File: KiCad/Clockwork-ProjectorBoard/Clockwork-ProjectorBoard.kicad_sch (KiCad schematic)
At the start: 32 parts, among them J1 to TCA955 PCB, J2 to DIN connecting 3+1 Socket 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, J3 to Lamp Relay Board, J4 to DIN Socket traces, J5 Relais Board, J6 uC Cable, J7 DIN-6 female, Q1 AO3400A, U1 AP63205WU, U3 TS5A3160DBVR-TP, U4 TS5A3160DBVR-TP, U5 TSV911ILT

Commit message: Renaming once more
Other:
- title: SynCrystal Projector Board T610/T525 -> Clockwork Projector Board T610/T525
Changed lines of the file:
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@@
 	(paper "A4")
 	(title_block
-		(title "SynCrystal Projector Board T610/T525")
-		(date "2025-02-11")
+		(title "Clockwork Projector Board T610/T525")
+		(date "2025-04-02")
 		(rev "Rev.A")
 		(company "filmkorn.org")

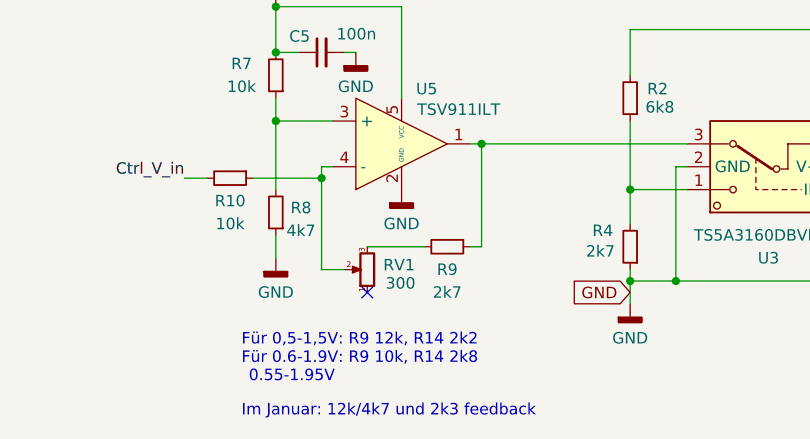
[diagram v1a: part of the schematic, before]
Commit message: New Gerbers, added the xtal to the BOM, new MH for OLED
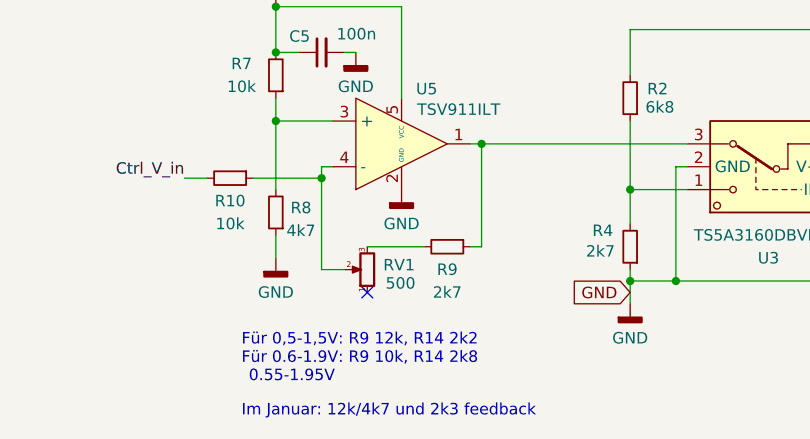
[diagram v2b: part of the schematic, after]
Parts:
- J2: LCSC C5188443 -> C6332196
- J6: footprint Connector_PinHeader_2.54mm:PinHeader_1x10_P2.54mm_Horizontal -> easyEDA:HDR-TH_10P-P2.54-H-M-W10.4_flipped; LCSC (none) -> C3012231
- R1: LCSC (none) -> C22962
- R2: LCSC (none) -> C23212
- R3: LCSC (none) -> C23189
- RV1: value 300 -> 500; LCSC C22461623 -> C720649; LCSC Part (none) -> C22461623
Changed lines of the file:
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@@
 			)
 		)
-		(property "LCSC" "C5188443"
+		(property "LCSC" "C6332196"
 			(at 57.15 33.02 0)
 			(effects
@@
 			)
 		)
-		(property "Datasheet" "~"
+		(property "Datasheet" "https://www.lcsc.com/datasheet/lcsc_datasheet_2411221126_UNI-ROYAL-Uniroyal-Elec-0603WAF2200T5E_C22962.pdf"
 			(at 223.52 119.38 0)
 			(effects
@@
 		)
 		(property "Description" ""
+			(at 223.52 119.38 0)
+			(effects
+				(font
+					(size 1.27 1.27)
+				)
+				(hide yes)
+			)
+		)
+		(property "LCSC" "C22962"
 			(at 223.52 119.38 0)
 			(effects
@@
 			)
 		)
-		(property "Value" "300"
+		(property "Value" "500"
 			(at 79.502 141.224 0)
 			(effects
@@
 			)
 		)
-		(property "Datasheet" "~"
+		(property "Datasheet" "https://www.lcsc.com/datasheet/lcsc_datasheet_2409302333_BOURNS-TC33X-2-501E_C720649.pdf"
 			(at 77.47 139.7 0)
 			(effects
@@
 			)
 		)
-		(property "LCSC" "C22461623"
+		(property "LCSC" "C720649"
+			(at 77.47 139.7 0)
+			(effects
+				(font
+					(size 1.27 1.27)
+				)
+				(hide yes)
+			)
+		)
+		(property "LCSC Part" "C22461623"
 			(at 77.47 139.7 0)
 			(effects
@@
 			)
 		)
-		(property "Footprint" "Connector_PinHeader_2.54mm:PinHeader_1x10_P2.54mm_Horizontal"
+		(property "Footprint" "easyEDA:HDR-TH_10P-P2.54-H-M-W10.4_flipped"
 			(at 254 138.43 0)
 			(effects
@@
 		)
 		(property "Description" "Generic connector, single row, 01x10, script generated"
+			(at 254 138.43 0)
+			(effects
+				(font
+					(size 1.27 1.27)
+				)
+				(hide yes)
+			)
+		)
+		(property "LCSC" "C3012231"
 			(at 254 138.43 0)
 			(effects
@@
 			)
 		)
+		(property "LCSC" "C23212"
+			(at 106.68 120.65 0)
+			(effects
+				(font
+					(size 1.27 1.27)
+				)
+				(hide yes)
+			)
+		)
 		(pin "1"
 		)
@@
 			(at 138.43 125.73 0)
 			(effects
+				(font
+					(size 1.27 1.27)
+				)
+				(hide yes)
+			)
+		)
+		(property "LCSC" "C23189"
+			(at 138.43 125.73 0)
+			(effects

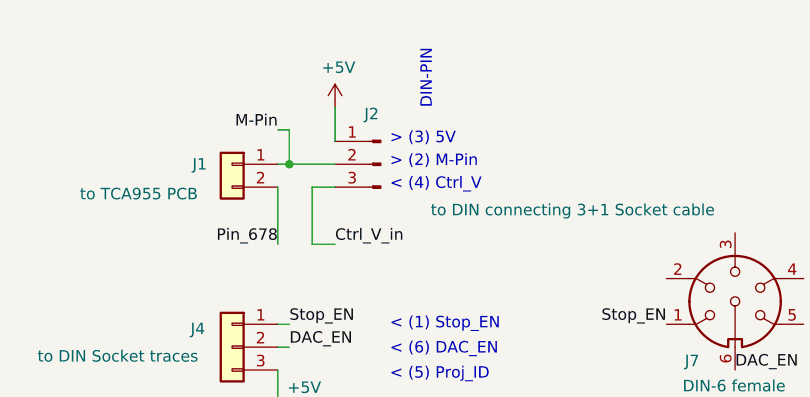
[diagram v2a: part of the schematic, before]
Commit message: Starting Rev.B, fixing DIN-Connector-Wire Pin 2/3 to keep DIN/JST pin alignment
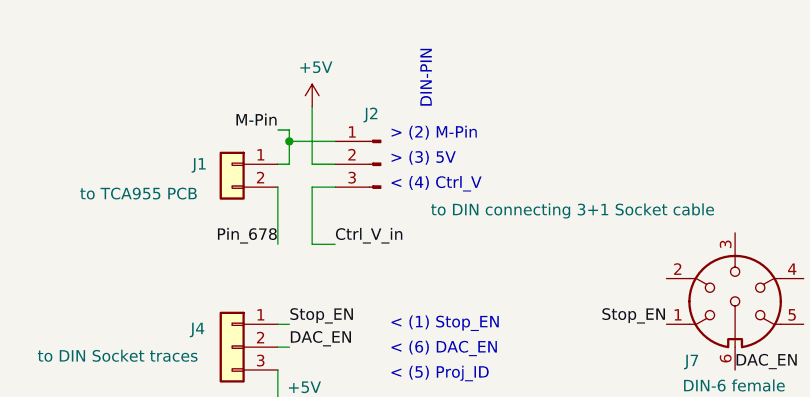
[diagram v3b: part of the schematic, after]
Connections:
- net +5V: now also J2.2 (Pin_2); no longer J2.1 (Pin_1)
- net M-Pin: now also J2.1 (Pin_1); no longer J2.2 (Pin_2)
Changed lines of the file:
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@@
 	)
 	(junction
-		(at 46.99 33.02)
-		(diameter 0)
-		(color 0 0 0 0)
-	)
-	(junction
 		(at 166.37 30.48)
 		(diameter 0)
@@
 	)
 	(junction
+		(at 46.99 30.48)
+		(diameter 0)
+		(color 0 0 0 0)
+	)
+	(junction
 		(at 167.64 130.81)
 		(diameter 0)
@@
 	(wire
 		(pts
-			(xy 90.17 125.73) (xy 88.9 125.73)
+			(xy 49.53 26.67) (xy 49.53 33.02)
 		)
 		(stroke
@@
 	(wire
 		(pts
-			(xy 246.38 114.3) (xy 246.38 121.92)
+			(xy 90.17 125.73) (xy 88.9 125.73)
 		)
 		(stroke
@@
 	(wire
 		(pts
-			(xy 254 102.87) (xy 254 133.35)
+			(xy 246.38 114.3) (xy 246.38 121.92)
 		)
 		(stroke
@@
 	(wire
 		(pts
-			(xy 172.72 30.48) (xy 173.99 30.48)
+			(xy 254 102.87) (xy 254 133.35)
 		)
 		(stroke
@@
 	(wire
 		(pts
-			(xy 46.99 33.02) (xy 52.07 33.02)
+			(xy 172.72 30.48) (xy 173.99 30.48)
 		)
 		(stroke
@@
 	(wire
 		(pts
+			(xy 46.99 30.48) (xy 46.99 33.02)
+		)
+		(stroke
+			(width 0)
+			(type default)
+		)
+	)
+	(wire
+		(pts
 			(xy 72.39 129.54) (xy 72.39 128.27)
 		)
@@
 	(wire
 		(pts
+			(xy 46.99 30.48) (xy 52.07 30.48)
+		)
+		(stroke
+			(width 0)
+			(type default)
+		)
+	)
+	(wire
+		(pts
 			(xy 72.39 128.27) (xy 73.66 128.27)
 		)
@@
 	(wire
 		(pts
+			(xy 49.53 33.02) (xy 52.07 33.02)
+		)
+		(stroke
+			(width 0)
+			(type default)
+		)
+	)
+	(wire
+		(pts
 			(xy 67.31 110.49) (xy 67.31 115.57)
 		)
@@
 	(wire
 		(pts
-			(xy 52.07 30.48) (xy 52.07 26.67)
-		)
-		(stroke
-			(width 0)
-			(type default)
-		)
-	)
-	(wire
-		(pts
 			(xy 143.51 43.18) (xy 152.4 43.18)
 		)
@@
 	(wire
 		(pts
-			(xy 46.99 29.21) (xy 46.99 33.02)
+			(xy 46.99 29.21) (xy 46.99 30.48)
 		)
 		(stroke
@@
 	(text "> (3) 5V"
 		(exclude_from_sim no)
-		(at 58.166 30.226 0)
+		(at 58.166 32.512 0)
 		(effects
 			(font
@@
 	(text "> (2) M-Pin"
 		(exclude_from_sim no)
-		(at 58.166 32.766 0)
+		(at 58.166 29.718 0)
 		(effects
 			(font
@@
 	(symbol
 		(lib_id "power:+5V")
-		(at 52.07 26.67 0)
+		(at 49.53 26.67 0)
 		(unit 1)
 		(exclude_from_sim no)
@@
 		(dnp no)
 		(property "Reference" "#PWR01"
-			(at 52.07 30.48 0)
+			(at 49.53 30.48 0)
 			(effects
 				(font
@@
 		)
 		(property "Value" "+5V"
-			(at 52.451 22.2758 0)
+			(at 49.911 22.2758 0)
 			(effects
 				(font
@@
 		)
 		(property "Footprint" ""
-			(at 52.07 26.67 0)
+			(at 49.53 26.67 0)
 			(effects
 				(font
@@
 		)
 		(property "Datasheet" ""
-			(at 52.07 26.67 0)
+			(at 49.53 26.67 0)
 			(effects
 				(font
@@
 		)
 		(property "Description" "Power symbol creates a global label with name \"+5V\""
-			(at 52.07 26.67 0)
+			(at 49.53 26.67 0)
 			(effects
 				(font

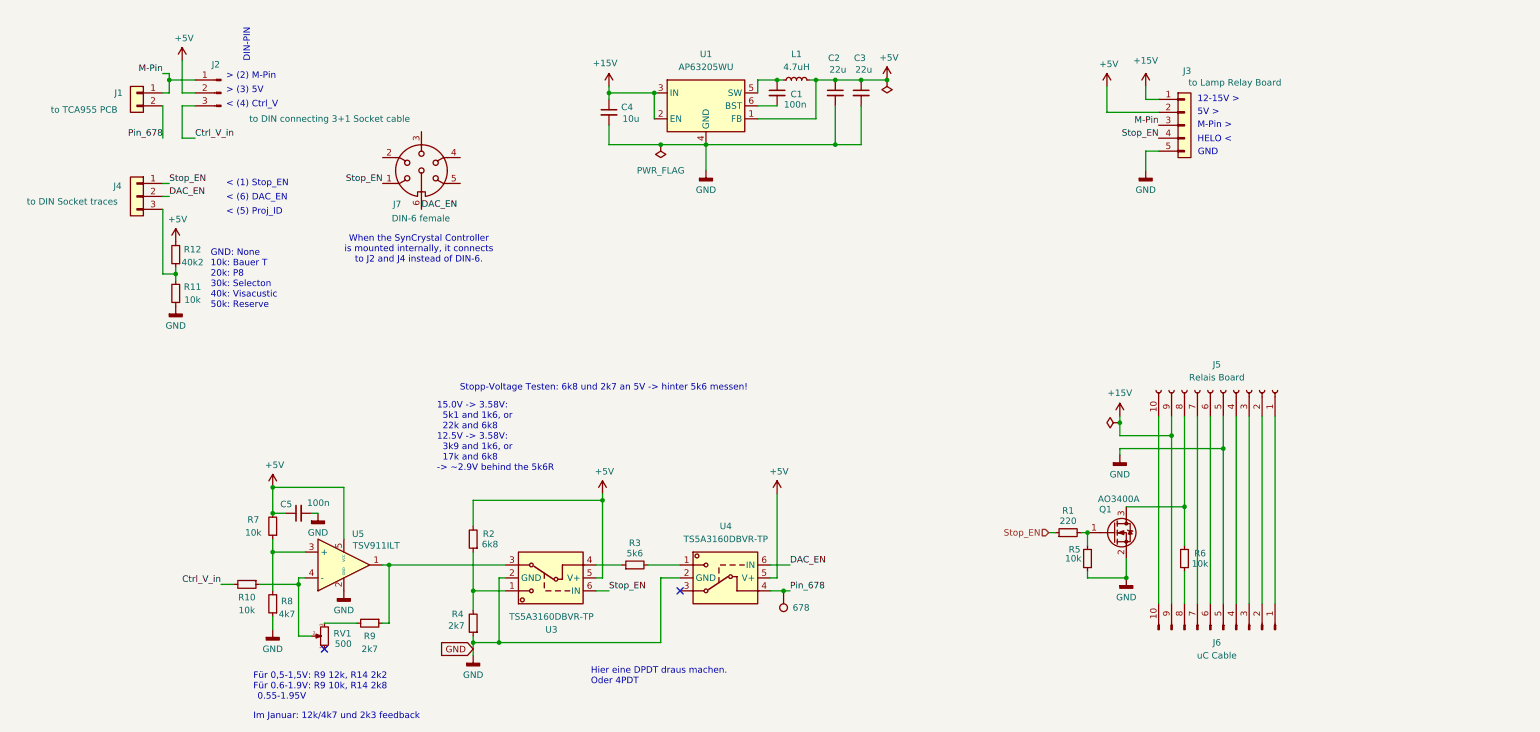
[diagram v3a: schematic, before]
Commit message: Fixes the Voltage Divider for the STOP Voltage, which turned out too low
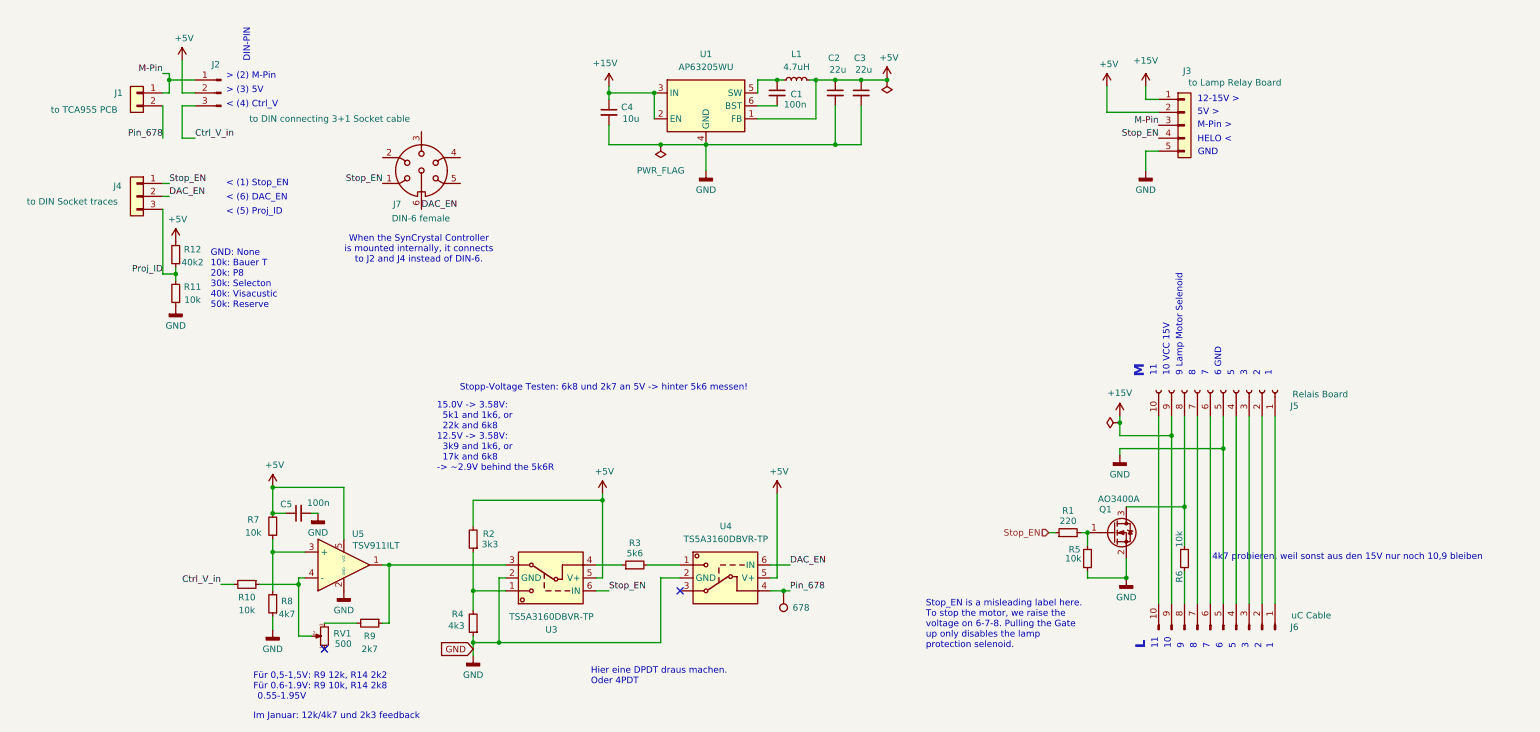
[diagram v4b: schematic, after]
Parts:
- R2: value 6k8 -> 3k3; LCSC C23212 -> (none)
- R4: value 2k7 -> 4k3; LCSC C13167 -> (none)
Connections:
- net Proj_ID: now reaches J4.3 (Pin_3), R11.2, R12.1
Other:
- note added: "1"
- note added: "10"
- note added: "10 VCC 15V"
- note added: "11"
- note added: "2"
- note added: "3"
- note added: "4k7 probieren, weil sonst aus den 15V nur noch 10,9 bleiben"
- note added: "5"
- note added: "6"
- note added: "6 GND"
- note added: "7"
- note added: "8"
- note added: "9"
- note added: "9 Lamp Motor Selenoid"
- note added: "L"
- note added: "M"
- note added: "Stop_EN is a misleading label here. To stop the motor, we raise the voltage on 6-7-8. Pulling the Gate up only disables the lamp protection selenoid."

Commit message: Adding a 6th Pin to the Lamp Relais Connector, which pulls the MOSFET high, disabling the built-in Relay
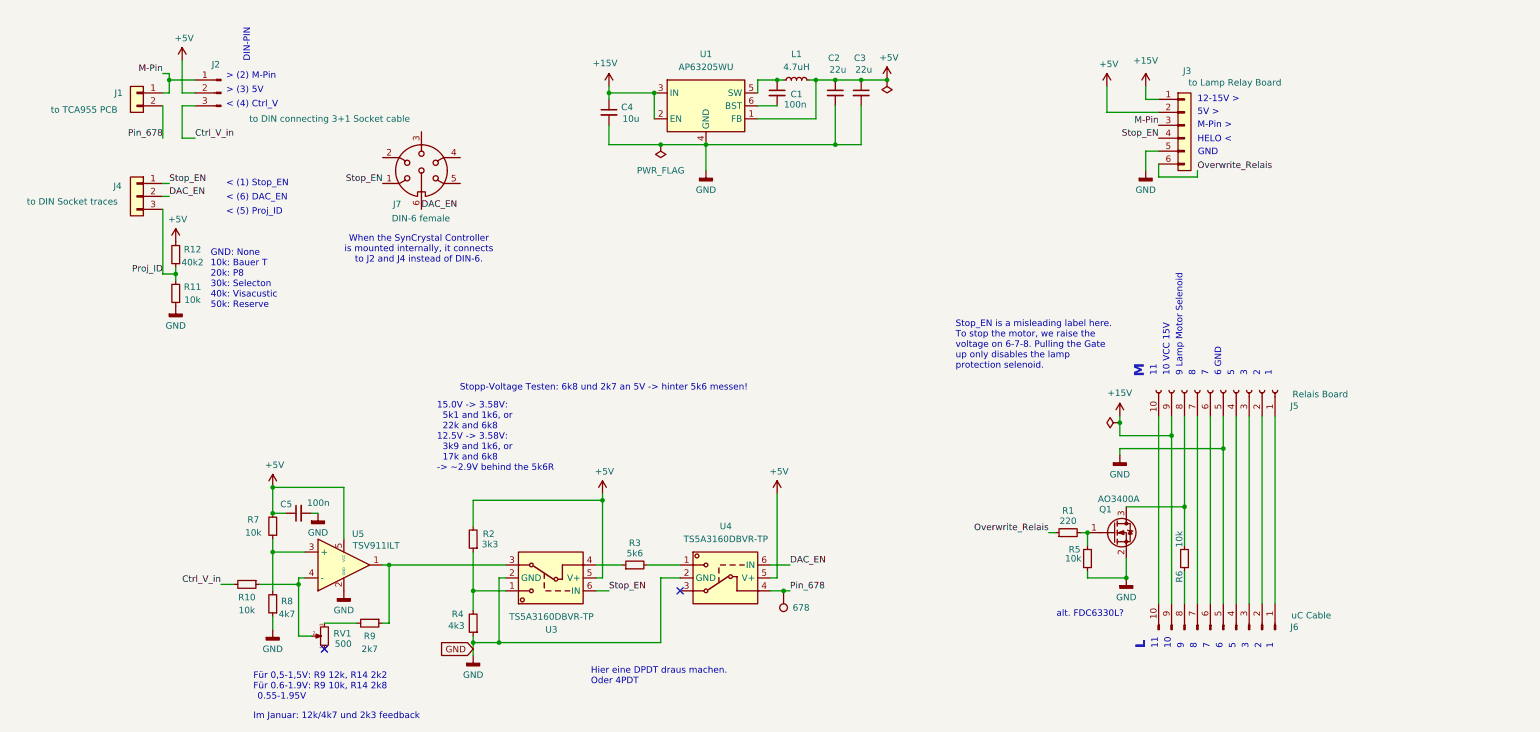
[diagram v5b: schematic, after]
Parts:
- J3: footprint easyEDA:CONN-TH_5P-P2.50_ZX-XH2.54-5PZZ -> easyEDA:CONN-TH_6P-P2.54_ZX-XH2.54-6PZZ-R; symbol Connector_Generic:Conn_01x05 -> Connector_Generic:Conn_01x06; LCSC C22388627 -> C22388628
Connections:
- net Stop_EN: no longer R1.1
- new net Overwrite_Relais: J3.6 (Pin_6), R1.1
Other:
- note added: "alt. FDC6330L?"
- note removed: "4k7 probieren, weil sonst aus den 15V nur noch 10,9 bleiben"
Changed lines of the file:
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@@
 	(wire
 		(pts
+			(xy 248.92 49.53) (xy 241.3 49.53)
+		)
+		(stroke
+			(width 0)
+			(type default)
+		)
+	)
+	(wire
+		(pts
 			(xy 238.76 44.45) (xy 241.3 44.45)
 		)
@@
 	(wire
 		(pts
+			(xy 241.3 49.53) (xy 241.3 46.99)
+		)
+		(stroke
+			(width 0)
+			(type default)
+		)
+	)
+	(wire
+		(pts
 			(xy 231.14 31.75) (xy 231.14 36.83)
 		)
@@
 	(wire
 		(pts
+			(xy 248.92 48.26) (xy 248.92 49.53)
+		)
+		(stroke
+			(width 0)
+			(type default)
+		)
+	)
+	(wire
+		(pts
 			(xy 233.68 97.79) (xy 233.68 100.33)
 		)
@@
 		)
 	)
+	(text "\n\n\n\n\n\n"
+		(exclude_from_sim no)
+		(at 214.63 118.11 0)
+		(effects
+			(font
+				(size 1.27 1.27)
+			)
+		)
+	)
 	(text "> (3) 5V"
 		(exclude_from_sim no)
@@
 	(text "Stop_EN is a misleading label here.\nTo stop the motor, we raise the \nvoltage on 6-7-8. Pulling the Gate\nup only disables the lamp \nprotection selenoid."
 		(exclude_from_sim no)
-		(at 195.58 137.414 0)
+		(at 201.422 82.55 0)
 		(effects
 			(font
@@
 		)
 	)
-	(text "4k7 probieren, weil sonst aus den 15V nur noch 10,9 bleiben"
-		(exclude_from_sim no)
-		(at 278.384 124.206 0)
-		(effects
-			(font
-				(size 1.27 1.27)
-			)
-		)
-	)
 	(text "GND: None\n10k: Bauer T\n20k: P8\n30k: Selecton\n40k: Visacustic\n50k: Reserve"
 		(exclude_from_sim no)
@@
 		)
 	)
+	(text "alt. FDC6330L?"
+		(exclude_from_sim no)
+		(at 227.838 135.382 0)
+		(effects
+			(font
+				(size 1.27 1.27)
+			)
+		)
+	)
 	(text "8"
 		(exclude_from_sim no)
@@
 		)
 	)
+	(label "Overwrite_Relais"
+		(at 219.71 119.38 180)
+		(effects
+			(font
+				(size 1.27 1.27)
+			)
+			(justify right bottom)
+		)
+	)
+	(label "Overwrite_Relais"
+		(at 248.92 48.26 0)
+		(effects
+			(font
+				(size 1.27 1.27)
+			)
+			(justify left bottom)
+		)
+	)
 	(label "Stop_EN"
 		(at 241.3 41.91 180)
@@
 		)
 	)
-	(hierarchical_label "Stop_EN"
-		(shape input)
-		(at 219.71 119.38 180)
-		(effects
-			(font
-				(size 1.27 1.27)
-			)
-			(justify right)
-		)
-	)
 	(symbol
 		(lib_id "power:GNDD")
@@
 	)
 	(symbol
-		(lib_id "Connector_Generic:Conn_01x05")
+		(lib_id "Connector_Generic:Conn_01x06")
 		(at 246.38 39.37 0)
 		(unit 1)
@@
 			)
 		)
-		(property "Footprint" "easyEDA:CONN-TH_5P-P2.50_ZX-XH2.54-5PZZ"
+		(property "Footprint" "easyEDA:CONN-TH_6P-P2.54_ZX-XH2.54-6PZZ-R"
 			(at 246.38 39.37 0)
 			(effects
@@
 			)
 		)
-		(property "Datasheet" "https://www.lcsc.com/datasheet/lcsc_datasheet_2410121306_Megastar-ZX-XH2-54-5PZZ-R_C22388627.pdf"
+		(property "Datasheet" "~"
 			(at 246.38 39.37 0)
 			(effects
@@
 			)
 		)
-		(property "Description" "Generic connector, single row, 01x05, script generated (kicad-library-utils/schlib/autogen/connector/)"
+		(property "Description" "Generic connector, single row, 01x06, script generated (kicad-library-utils/schlib/autogen/connector/)"
 			(at 246.38 39.37 0)
 			(effects
@@
 			)
 		)
-		(property "LCSC" "C22388627"
+		(property "LCSC" "C22388628"
 			(at 246.38 39.37 0)
 			(effects
@@
 		(pin "5"
 		)
+		(pin "6"
+		)
 		(instances
